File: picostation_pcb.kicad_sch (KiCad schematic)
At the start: 13 parts, among them J1 Conn_01x06_Female, J2 Conn_01x20_Female, J3 PICO, J4 Conn_02x10_Female, U1 LM78M05_TO252

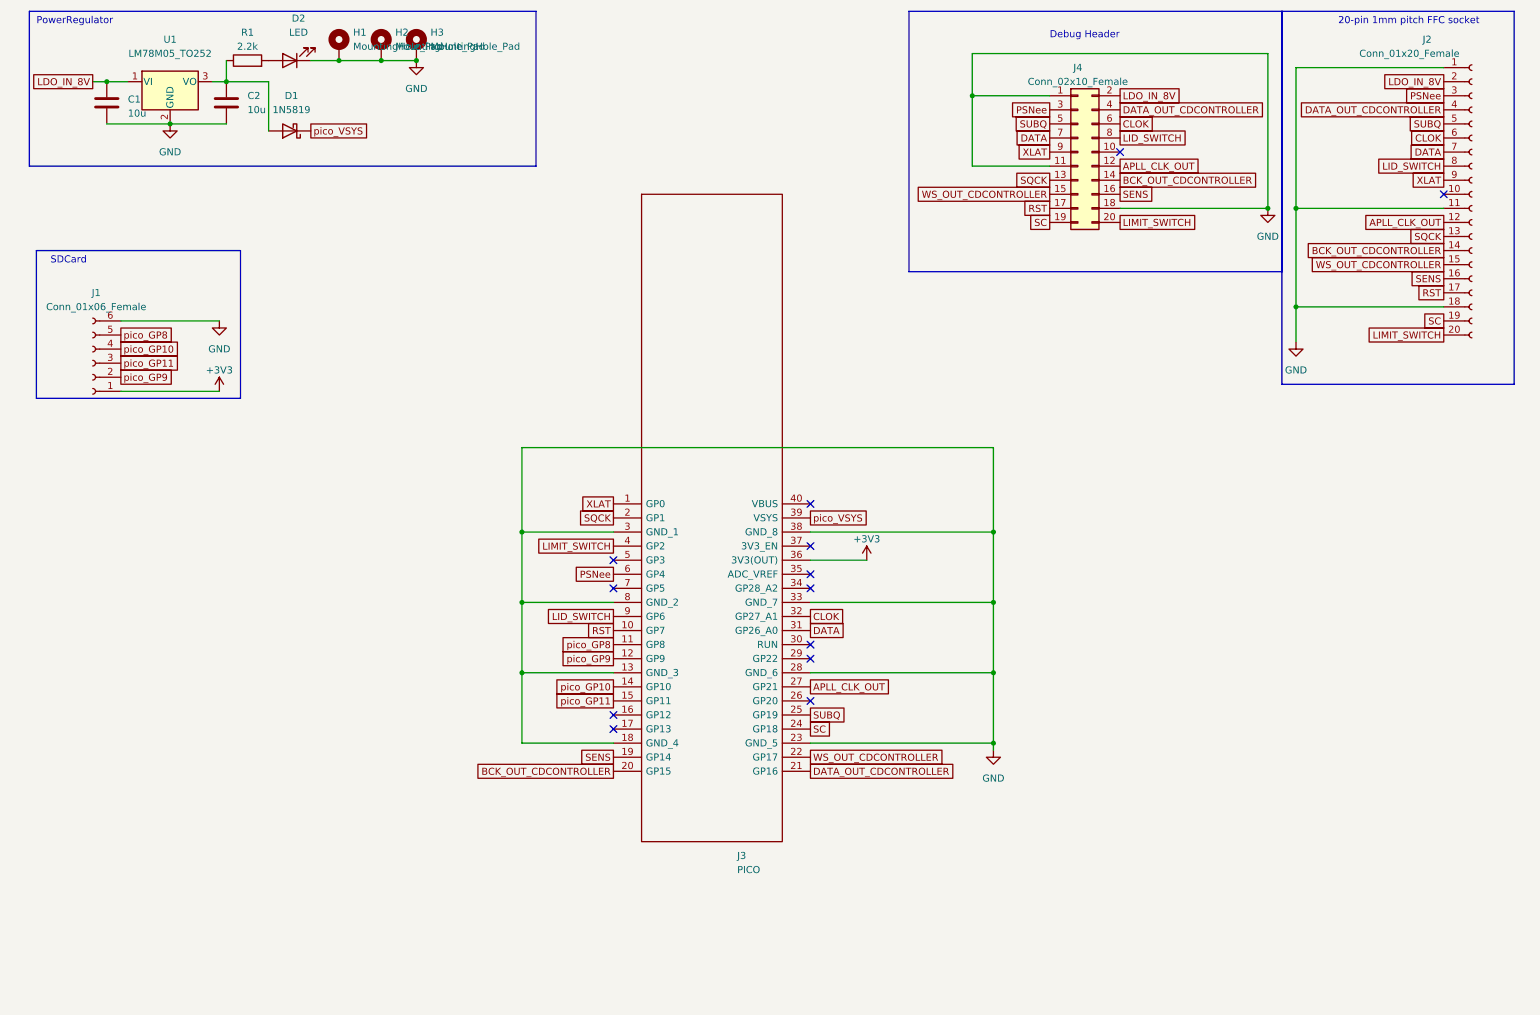
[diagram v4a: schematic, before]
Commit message: Change Label Names for MicroSD Pins
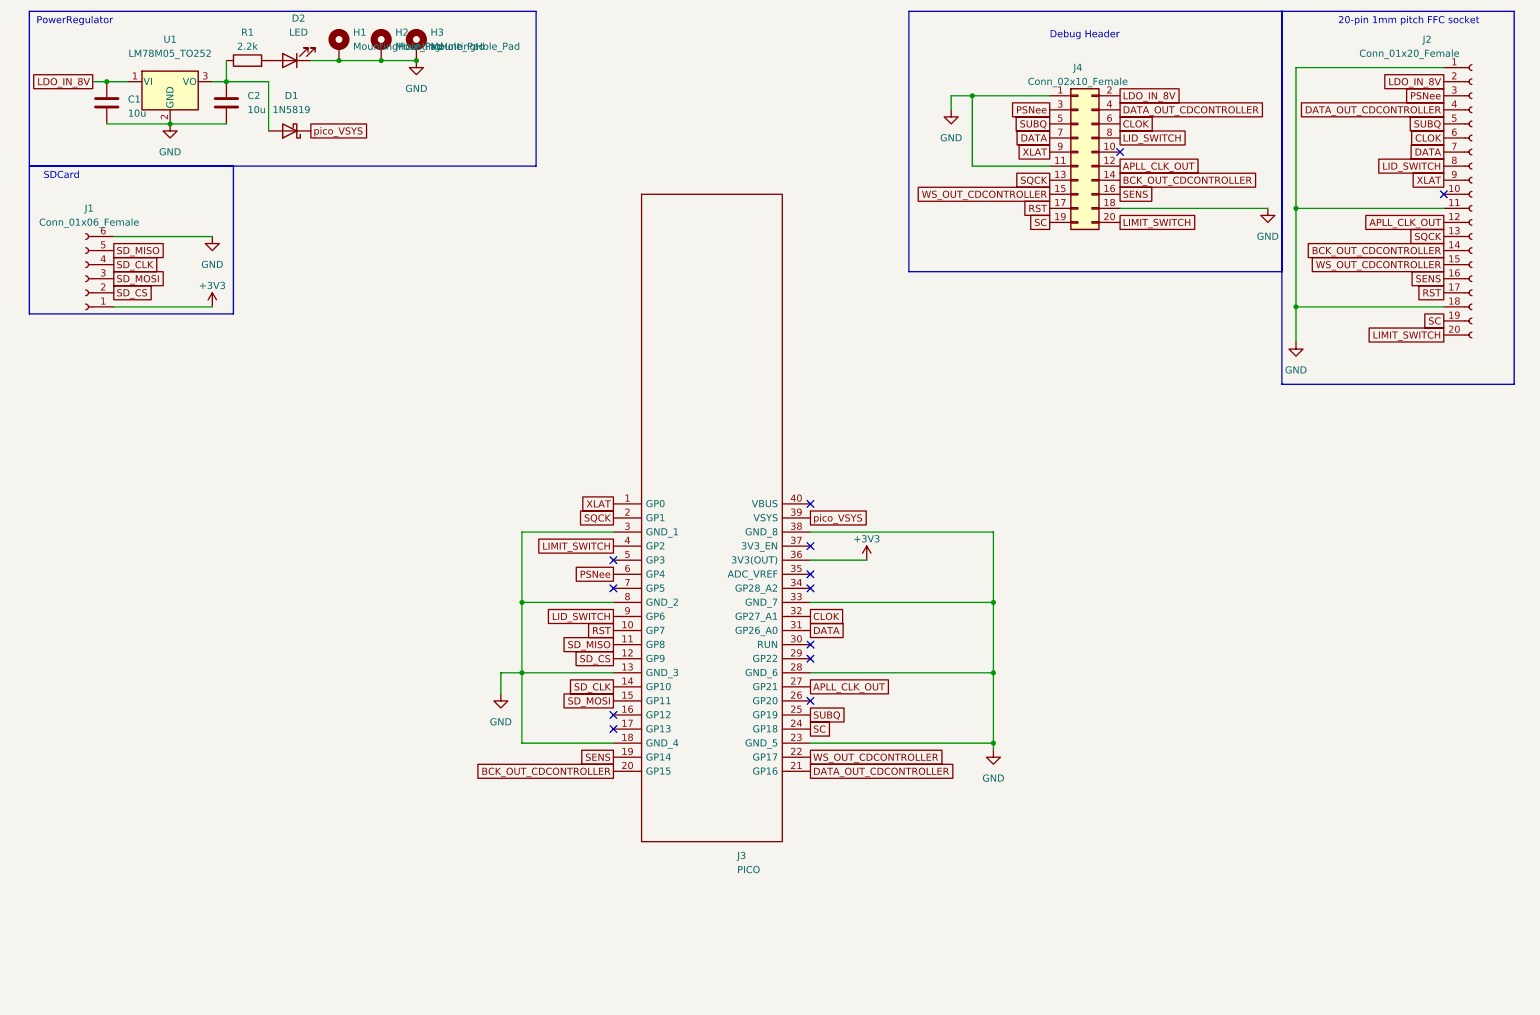
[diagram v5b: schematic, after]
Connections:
- net pico_GP10 renamed SD_CLK
- net pico_GP11 renamed SD_MOSI
- net pico_GP8 renamed SD_MISO
- net pico_GP9 renamed SD_CS
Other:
- moved on the sheet: J1
